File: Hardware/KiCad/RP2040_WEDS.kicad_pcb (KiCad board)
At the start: 2 copper layers, 55 x 66 mm, 82 parts, among them J2 USB BOOT, J3 I2C Soil Header, J4 LiPo Batt, J5 Analog Soil Header, J6 USB Header, J7 SWD Header, J8 SMA-Conn, J9 Solar Panel Input, Q1 Q_PMOS_DGS, Q2 Q_PMOS_DGS, SW1 SW_Push, SW2 SW_Push, SW3 SW_Push, U1 RP2040, U2 MCP73831-2-OT, U3 W25Q128JVS, U4 BME280, U5 XC6210B332MR, U6 LoRa-E5, U7 TPL5110, Y1 Crystal_GND24

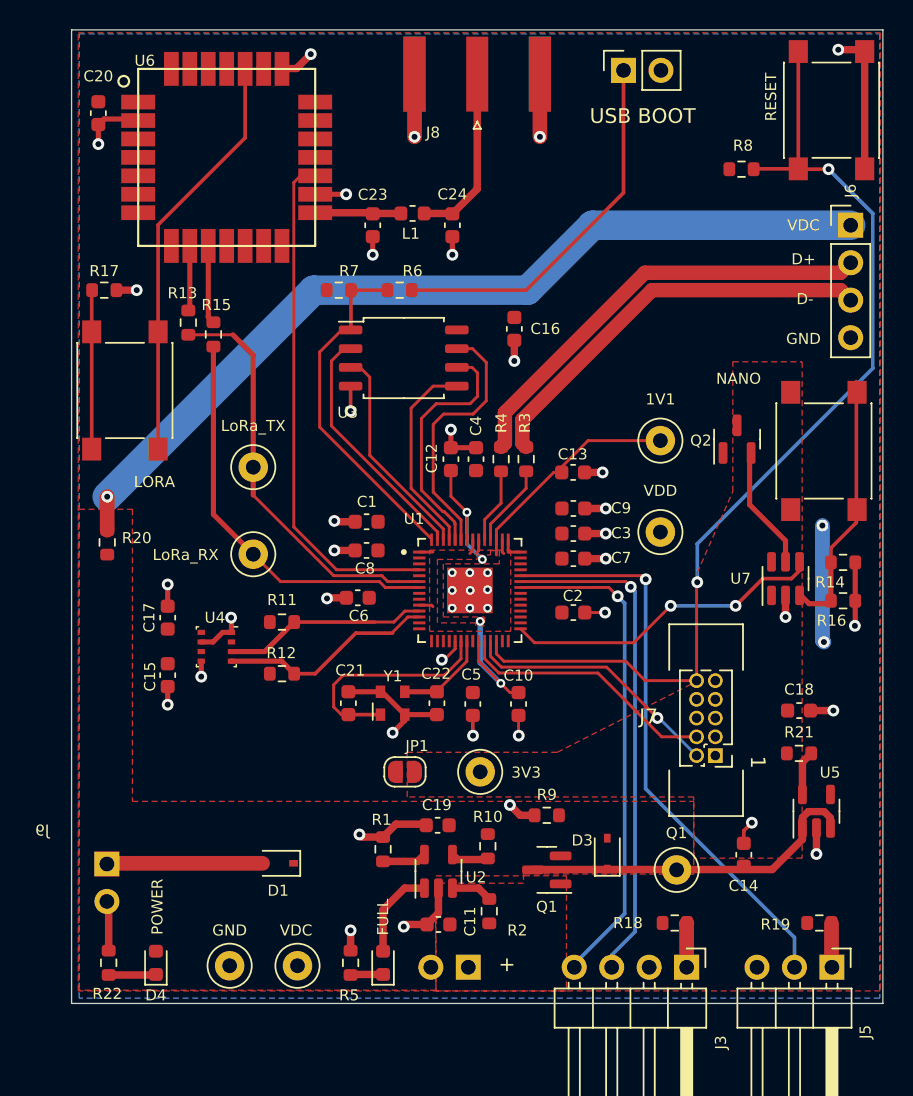
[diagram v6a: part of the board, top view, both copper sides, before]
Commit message: added lables and boxes to schematic
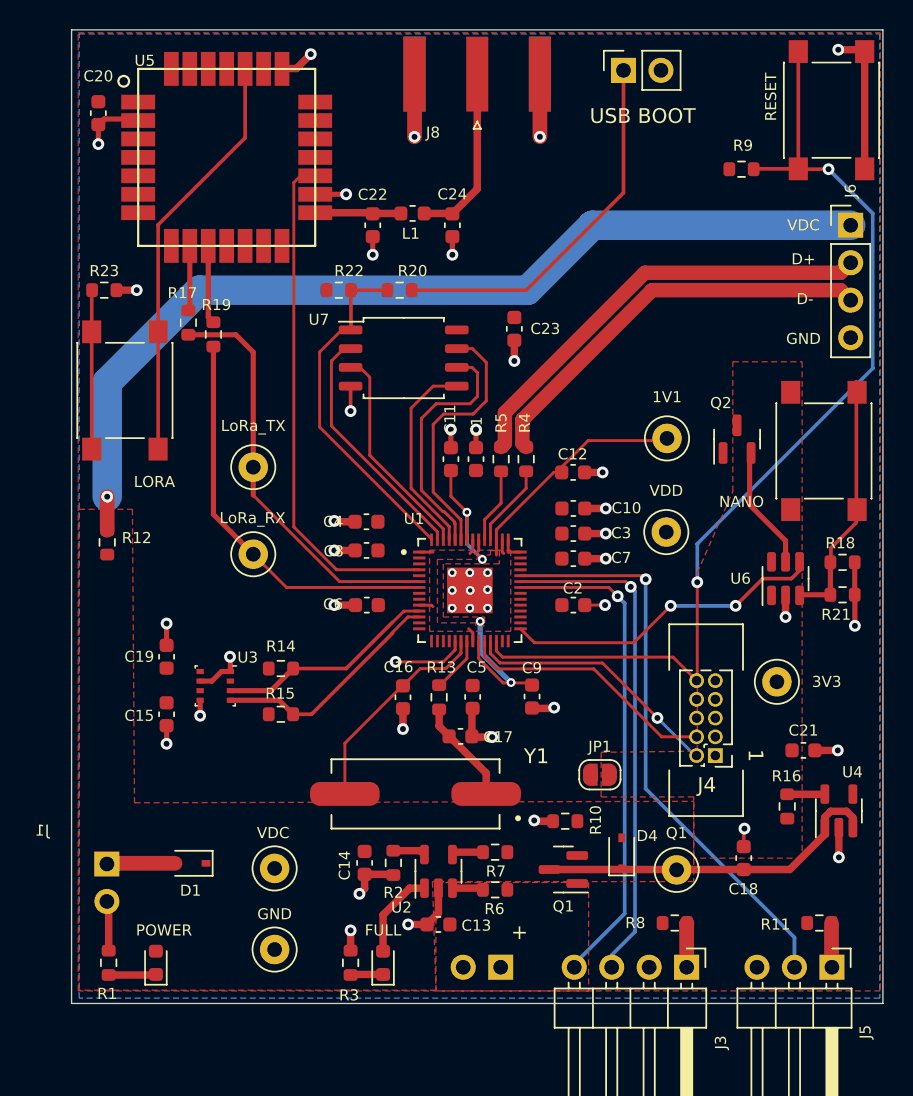
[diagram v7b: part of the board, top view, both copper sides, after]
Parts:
- removed the C21 at (138.6, 113.7)
- removed the C22 at (144.6, 113.7)
- added C16: 27pF, Capacitor_SMD:C_0603_1608Metric, F.Cu at (142.3, 113.3)
- added C17: 27pF, Capacitor_SMD:C_0603_1608Metric, F.Cu at (146.2, 116.0)
- added R13: 1k, Resistor_SMD:R_0603_1608Metric, F.Cu at (144.7, 113.3)
- R22: renamed from R7; value 10k -> DNP
- Y1: value Crystal_GND24 -> 12MHz Crystal; footprint Oscillator:Oscillator_SMD_Abracon_ASDMB-4Pin_2.5x2.0mm -> 54-00125:XTAL1140X470X420N
- moved TP1 21.0 mm to (167.6, 112.2)
- moved JP1 13.2 mm to (155.6, 118.5)
- moved C4 8.55 mm to (139.8, 101.4), turned to 180 degrees
- moved C1 8.55 mm to (147.2, 97.2), turned to 90 degrees
- moved TP5 6.78 mm to (133.6, 124.9)
- moved Y1 6.34 mm to (143.1, 119.8), turned to 180 degrees
- moved D1 5.94 mm to (127.9, 124.6)
- moved C14 5.57 mm to (139.7, 124.5), turned to -90 degrees
- moved R16 3.69 mm to (168.3, 120.7), turned to 90 degrees
- moved TP3 3.24 mm to (133.6, 130.4)
- moved R14 3.15 mm to (134.0, 111.3)
- moved R15 2.75 mm to (134.0, 114.5)
- moved C21 2.72 mm to (169.4, 116.9)
- moved U3 2.65 mm to (129.6, 112.5)
- moved C15 2.65 mm to (126.3, 114.5)
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- renumbered C9 to C10, C12 to C11, C13 to C12, C11 to C13, C19 to C14, C14 to C18, C17 to C19, C18 to C21, C23 to C22, C16 to C23, C10 to C9, D4 to D2, D2 to D3, D3 to D4, J9 to J1, J4 to J2, J7 to J4, J2 to J7, R22 to R1, R9 to R10, R19 to R11, R20 to R12, R11 to R14, R12 to R15, R21 to R16, R13 to R17, R14 to R18, R15 to R19, R1 to R2, R6 to R20, R16 to R21, R17 to R23, R5 to R3, R3 to R4, R4 to R5, R2 to R6, R10 to R7, R18 to R8, R8 to R9, TP4 to TP3, TP5 to TP4, TP3 to TP5, TP8 to TP6, TP6 to TP7, TP7 to TP8, U4 to U3, U5 to U4, U6 to U5, U7 to U6, U3 to U7
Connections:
- net /D+ renamed Net-(R5-Pad1)
- net /D- renamed Net-(R4-Pad1)
- Y1 pad 1: XIN -> Net-(C17-Pad2)
- Y1 pad 2: GND -> XIN
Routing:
- net VDD: track 14.5 -> 7.55 mm, vias 2 -> 0
- net Net-(C17-Pad2): track 0.00 -> 6.50 mm
- net Net-(D1-Pad2): track 10.6 -> 4.64 mm
- net Net-(J6-Pad1): track 60.3 -> 64.8 mm
- net GND: track 93.2 -> 88.8 mm, vias 46 -> 47
- net XOUT: track 5.91 -> 3.81 mm
- net SCL: track 14.7 -> 16.0 mm
- net +1V1: track 34.0 -> 35.1 mm
- net SDA: track 13.9 -> 14.9 mm
- net XIN: track 15.5 -> 14.7 mm
- net Net-(R2-Pad2): track 3.00 -> 2.21 mm
- net Net-(R18-Pad2): track 18.0 -> 17.2 mm
- net Net-(R6-Pad2): track 2.80 -> 2.12 mm

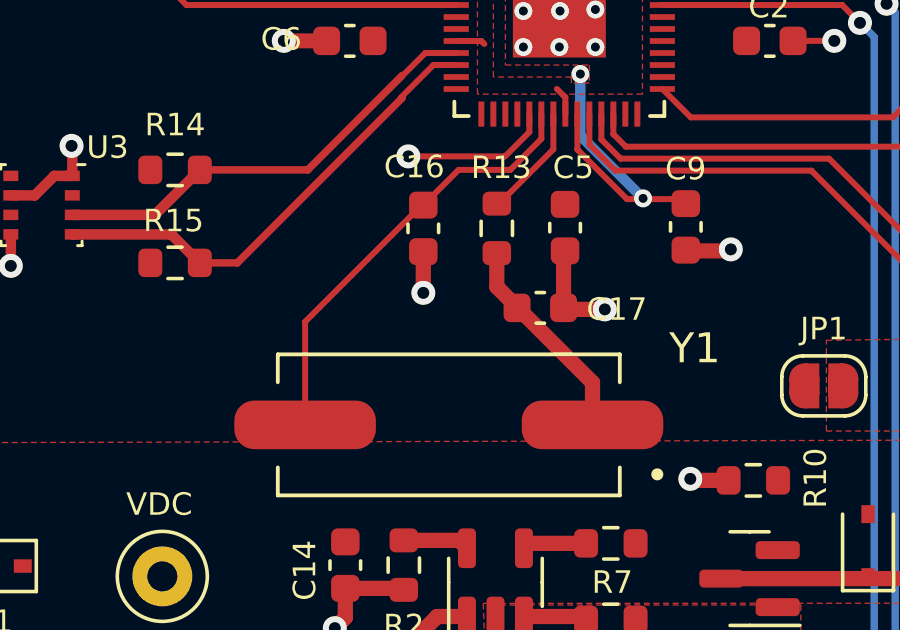
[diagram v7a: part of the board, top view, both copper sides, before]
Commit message: fixed traces
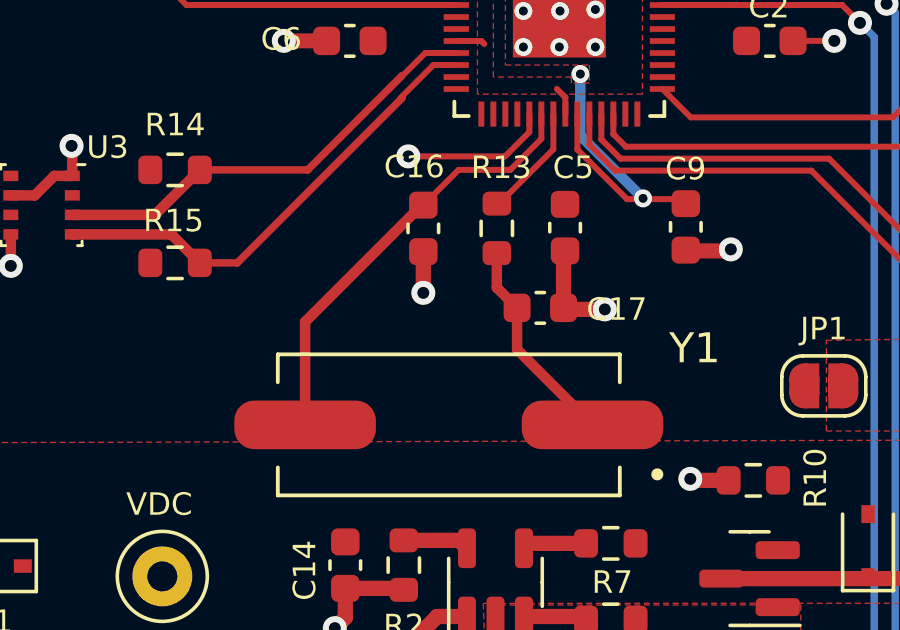
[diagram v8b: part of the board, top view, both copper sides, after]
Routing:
- net Net-(C17-Pad2): track 6.50 -> 7.05 mm
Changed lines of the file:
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@@
   (segment (start 145.195 111.35) (end 143.47 111.35) (width 0.2) (layer "F.Cu") (net 4))
   (segment (start 146.23 109.49) (end 146.23 110.315) (width 0.2) (layer "F.Cu") (net 4))
-  (segment (start 142.245 112.525) (end 138.355 116.415) (width 0.2) (layer "F.Cu") (net 4))
+  (segment (start 142.245 112.525) (end 138.355 116.415) (width 0.35) (layer "F.Cu") (net 4))
   (segment (start 143.47 111.35) (end 142.295 112.525) (width 0.2) (layer "F.Cu") (net 4))
   (segment (start 142.295 112.525) (end 142.245 112.525) (width 0.2) (layer "F.Cu") (net 4))
   (segment (start 146.23 110.315) (end 145.195 111.35) (width 0.2) (layer "F.Cu") (net 4))
-  (segment (start 138.355 116.415) (end 138.355 119.85) (width 0.2) (layer "F.Cu") (net 4))
+  (segment (start 138.355 116.415) (end 138.355 119.85) (width 0.35) (layer "F.Cu") (net 4))
   (segment (start 146.63 110.665) (end 144.82 112.475) (width 0.2) (layer "F.Cu") (net 5))
   (segment (start 144.82 112.475) (end 144.745 112.475) (width 0.2) (layer "F.Cu") (net 5))
@@
   (segment (start 125.695 88.525) (end 125.695 96.475) (width 0.25) (layer "F.Cu") (net 61))
   (segment (start 125.695 88.525) (end 125.695 81.274511) (width 0.25) (layer "F.Cu") (net 61))
-  (segment (start 144.745 114.125) (end 144.745 115.25) (width 0.508) (layer "F.Cu") (net 62))
-  (segment (start 144.745 115.25) (end 147.935 118.44) (width 0.508) (layer "F.Cu") (net 62))
-  (segment (start 147.935 118.44) (end 147.935 119.3) (width 0.508) (layer "F.Cu") (net 62))
+  (segment (start 144.745 115.275) (end 145.42 115.95) (width 0.35) (layer "F.Cu") (net 62))
+  (segment (start 144.745 114.125) (end 144.745 115.275) (width 0.35) (layer "F.Cu") (net 62))
+  (segment (start 145.42 115.95) (end 145.42 117.335) (width 0.35) (layer "F.Cu") (net 62))
+  (segment (start 145.42 117.335) (end 147.935 119.85) (width 0.35) (layer "F.Cu") (net 62))
   (segment (start 172.795 121.45) (end 172.795 122.1375) (width 0.5) (layer "F.Cu") (net 63))
   (segment (start 171.29452 121.02548) (end 172.37048 121.02548) (width 0.5) (layer "F.Cu") (net 63))
